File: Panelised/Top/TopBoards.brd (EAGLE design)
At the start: 120.7 x 66.5 mm, 30 parts, among them K1 HF46105, K11 61004021821, K2 HF46105, K3 HF46105, K4 HF46105, P1 DF11-06-2DSA, Q1 691131710002, Q11 BS170, Q2 691131710002, Q3 691131710002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

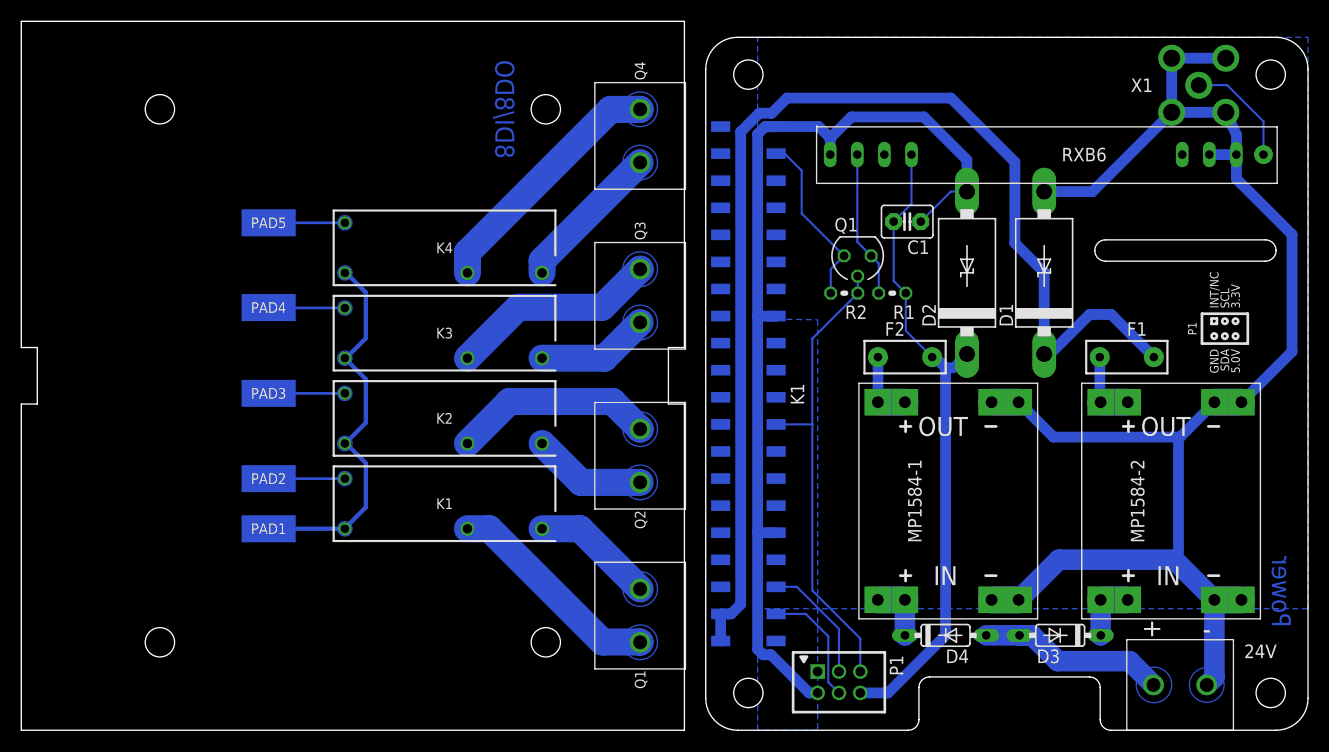
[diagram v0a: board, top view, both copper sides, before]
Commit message: Remove Schottky - Diodes, since already on DC/DC buck converter.
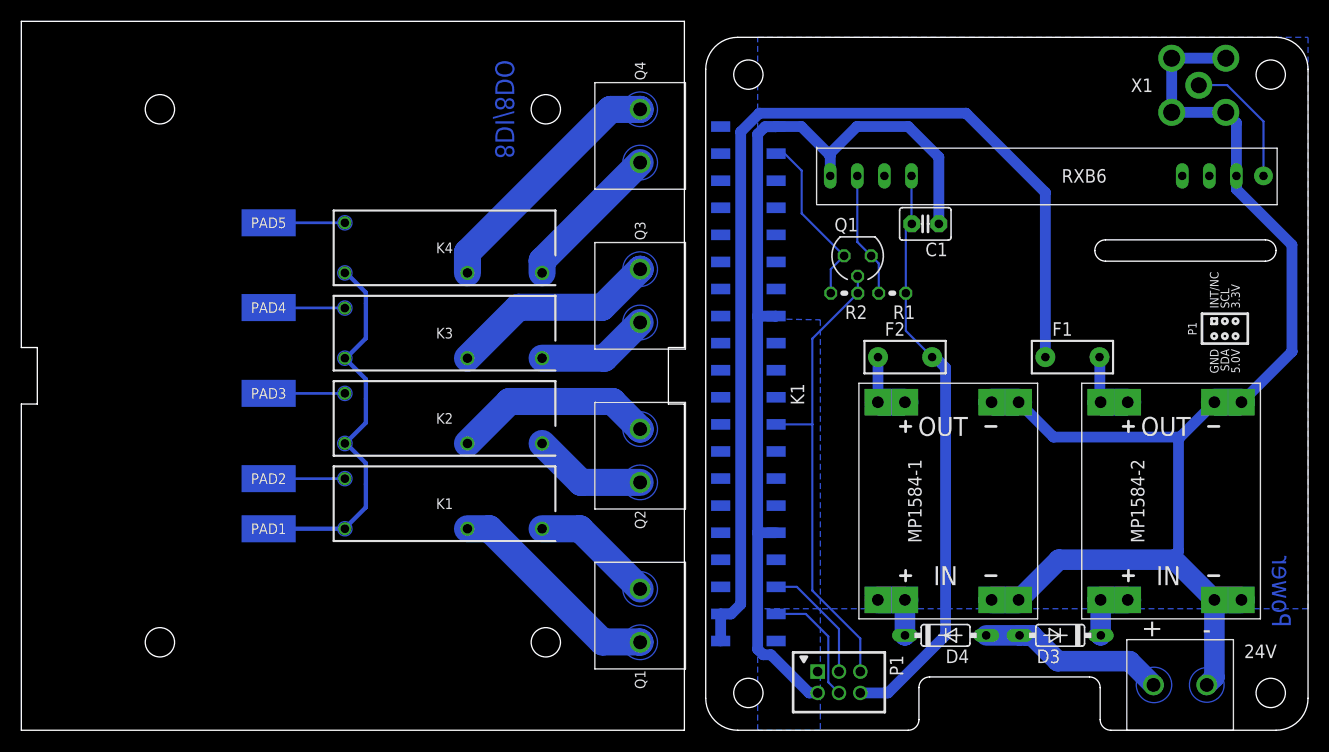
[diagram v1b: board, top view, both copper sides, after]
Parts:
- removed D1, D2: 1N5908, diode:C4111-15
- moved F1 5.10 mm to (36.4, 35.0), turned to 0 degrees
- moved RXB6 2.00 mm to (34.0, 52.0)
- moved C1 1.71 mm to (22.6, 47.5)
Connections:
- net GND: no longer D1.A, D2.A
- net N$21: no longer D2.C
- net N$51: no longer D1.C
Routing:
- net GND: track 229.3 -> 208.0 mm
- net N$51: track 111.3 -> 96.9 mm
- net N$21: track 60.8 -> 55.3 mm
- net N$81: track 10.6 -> 12.6 mm
- net N$3: track 13.8 -> 11.8 mm

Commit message: Revert "Remove Schottky - Diodes, since already on DC/DC buck converter."
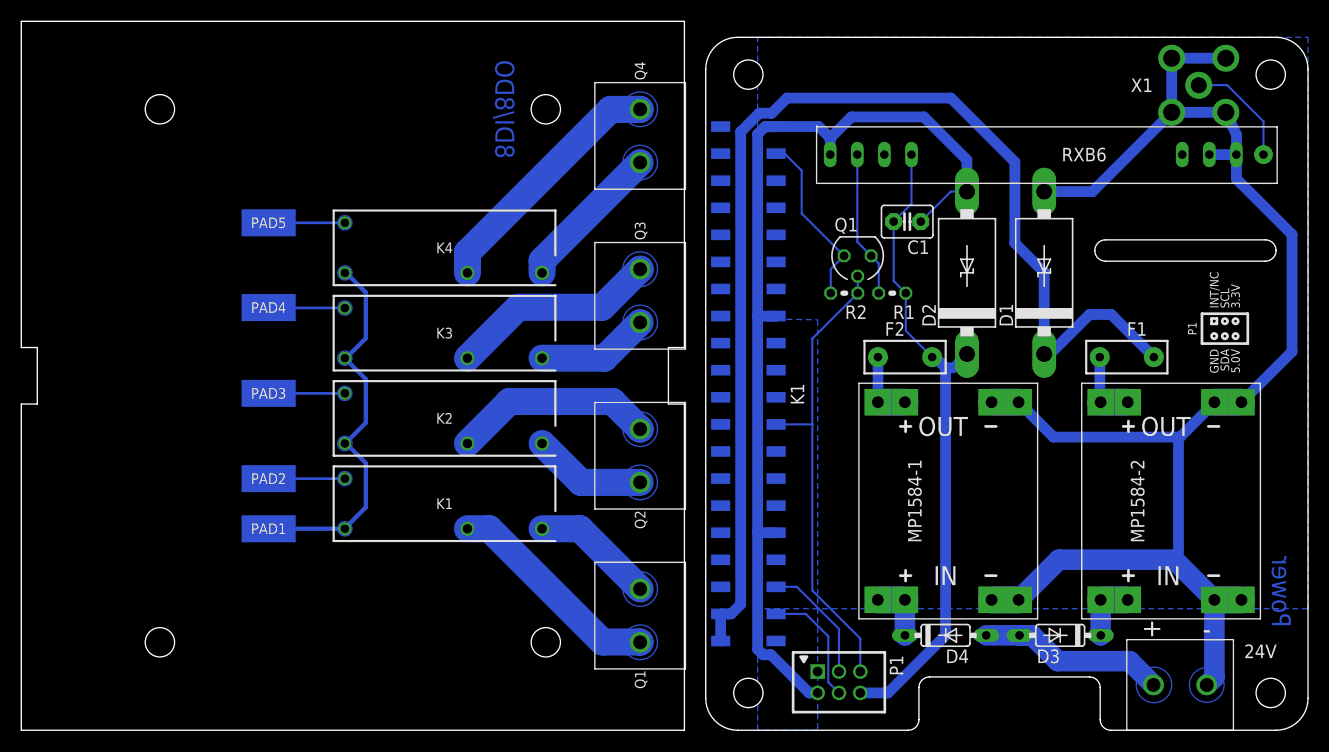
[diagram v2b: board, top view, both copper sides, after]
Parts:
- added D1, D2: 1N5908, diode:C4111-15
- moved F1 5.10 mm to (41.5, 35.0), turned to 180 degrees
- moved RXB6 2.00 mm to (34.0, 54.0)
- moved C1 1.71 mm to (20.9, 47.7)
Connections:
- net GND: now also D1.A, D2.A
- net N$21: now also D2.C
- net N$51: now also D1.C
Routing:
- net GND: track 208.0 -> 229.3 mm
- net N$51: track 96.9 -> 111.3 mm
- net N$21: track 55.3 -> 60.8 mm
- net N$81: track 12.6 -> 10.6 mm
- net N$3: track 11.8 -> 13.8 mm
